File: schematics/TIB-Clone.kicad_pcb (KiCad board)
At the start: 2 copper layers, 91.4 x 58.4 mm, 27 parts, among them CN1 FLOPPY CONNECTOR, J1 MO1, J2 MO2, J3 DS1, J4 DS2, Q1 16.000, U1 2764, U2 74LS00, U3 74LS00, U4 WD37C65

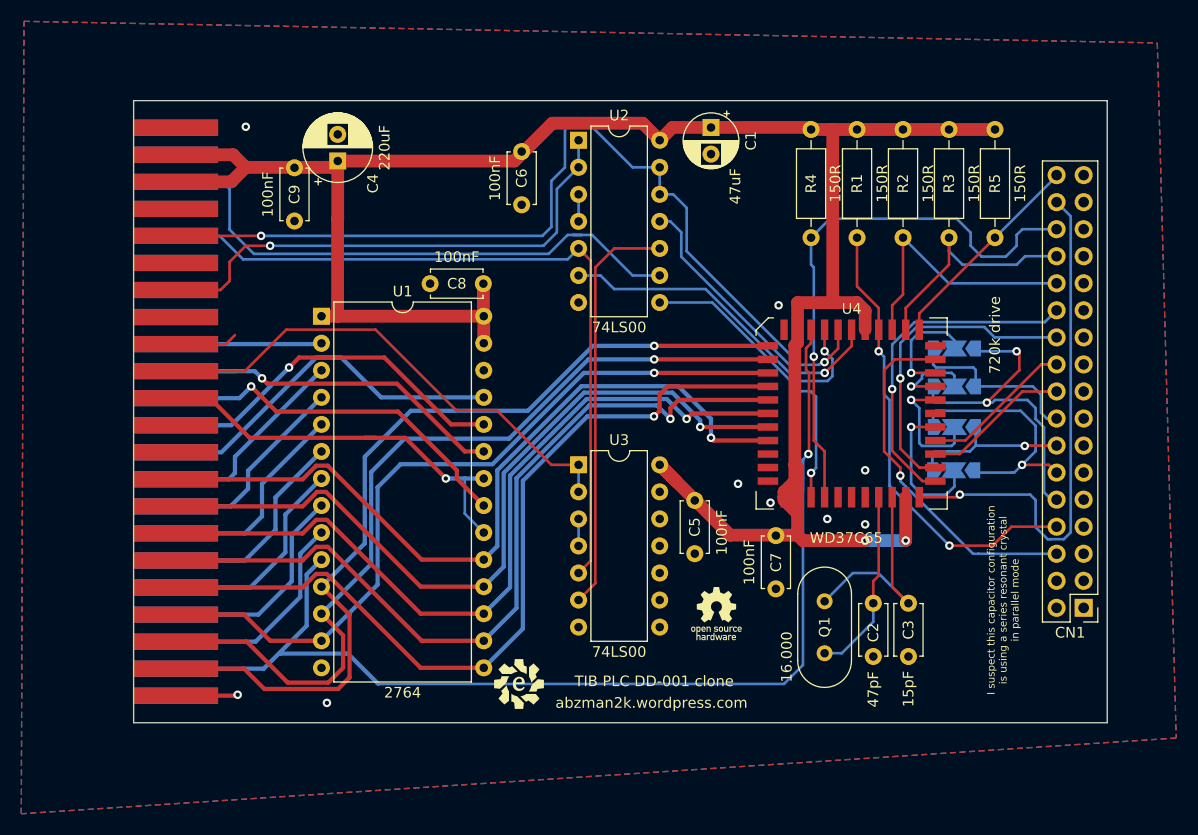
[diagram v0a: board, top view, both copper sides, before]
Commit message: changed to through hole socket and through hole jumpers, fixed typo and added optional mounting hole
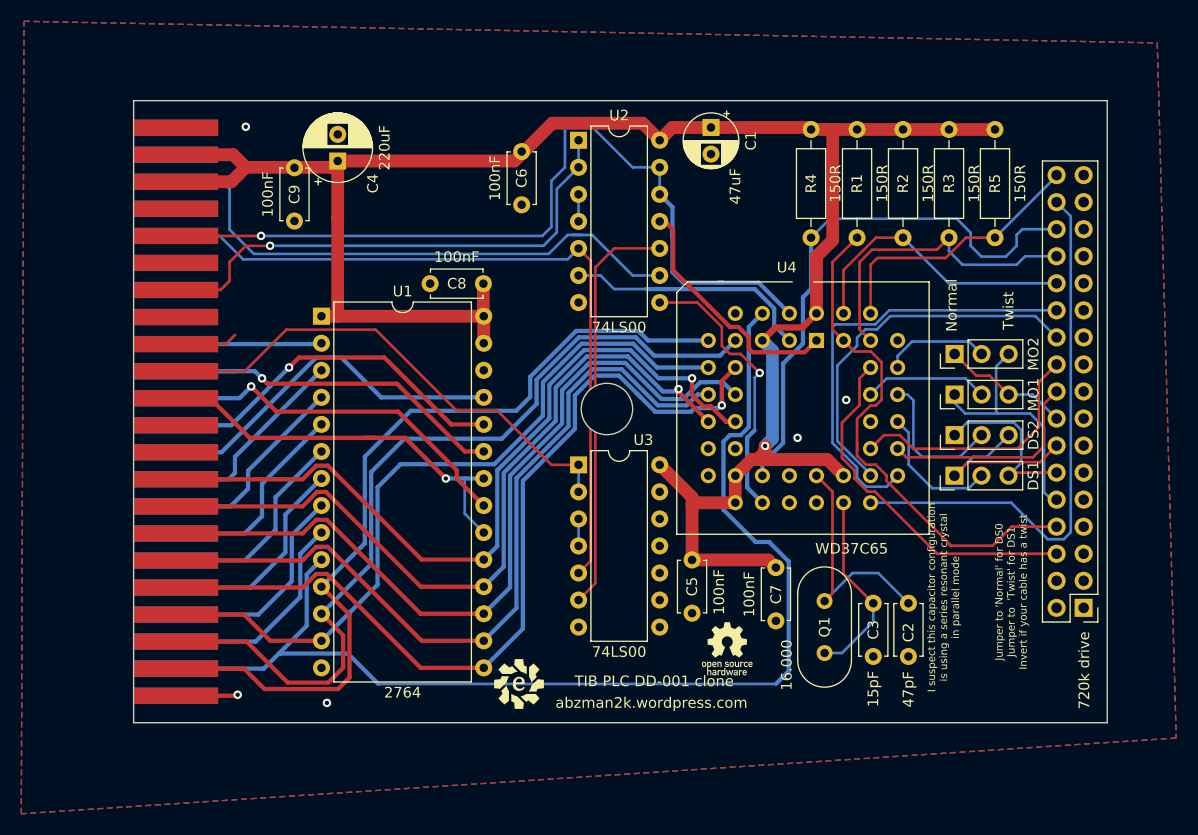
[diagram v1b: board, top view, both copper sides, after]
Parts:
- added ?: , , F.Cu at (174.1, 76.0)
- J1, J2, J3, J4: footprint Jumper:SolderJumper-3_P2.0mm_Open_TrianglePad1.0x1.5mm_NumberLabels -> Connector_PinHeader_2.54mm:PinHeader_1x03_P2.54mm_Vertical; moved to F.Cu
- U4: footprint Package_LCC:PLCC-44 -> Package_LCC:PLCC-44_THT-Socket
- moved U4 7.61 mm to (193.8, 69.6)
- moved C5 5.59 mm to (182.1, 90.2)
- moved Q1 4.90 mm to (194.6, 94.1), turned to -90 degrees
- moved G*** 3.45 mm to (185.4, 98.6)
- moved C2 3.30 mm to (202.4, 99.3)
- moved C3 3.30 mm to (199.1, 99.3)
- moved C7 3.01 mm to (190.0, 90.9)
- moved J1 0.76 mm to (206.8, 74.7), turned to 90 degrees
- moved J4 0.76 mm to (206.8, 78.5), turned to 90 degrees
- moved J3 0.51 mm to (206.8, 82.3), turned to 90 degrees
- moved J2 0.51 mm to (206.8, 70.9), turned to 90 degrees
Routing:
- net +5V: track 231.8 -> 195.7 mm, vias 2 -> 1
- net *STEP: track 14.4 -> 24.3 mm
- net *WE: track 32.0 -> 41.4 mm, vias 1 -> 0
- net Net-(CN1-Pad12): track 24.1 -> 16.5 mm, vias 1 -> 0
- net Net-(CN1-Pad10): track 31.3 -> 23.8 mm, vias 2 -> 0
- net *WP: track 22.6 -> 29.4 mm
- net *FWR: track 86.8 -> 80.1 mm, vias 2 -> 1
- net *DIRC: track 13.8 -> 20.2 mm
- net *IDX: track 43.3 -> 49.6 mm, vias 2 -> 0
- net *WD: track 29.6 -> 35.4 mm, vias 1 -> 0
- net *DCHG: track 19.9 -> 25.6 mm
- net Net-(C2-Pad2): track 17.7 -> 22.8 mm
- net Net-(CN1-Pad16): track 17.1 -> 12.3 mm
- net *FRD: track 27.8 -> 23.1 mm, vias 1 -> 0
- net *FCS: track 32.8 -> 28.8 mm, vias 1 -> 0
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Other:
- board text added: "Based on work from Steve Gray, Jan Pedersen, and Josef at ide64.org"
- board text added: "Jumper to 'Normal' for DS0 Jumper to 'Twist' for DS1 Invert if your cable has a twist"
- board text removed: "Based on work from Steve Gary, Jan Pedersen, and Josef at ide64.org"
- board text removed: "Jumper to 'Normal' if you have a drive set for DS0 Jumper to 'Twist' if you have a drive set to DS1 Invert both of these instructions if your cable has a twist"
